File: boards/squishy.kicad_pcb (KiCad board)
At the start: 4 copper layers, 82 x 76.8 mm, 173 parts, among them J1 USB_B_Micro, J2 Conn_02x26_Top_Bottom, J3 Conn_02x05_Odd_Even, U1 128MiB, U10 THVD1451, U11 THVD1451, U12 THVD1451, U13 THVD1451, U14 THVD1451, U15 THVD1451, U16 THVD1451, U17 THVD1451, U18 THVD1451, U19 THVD1451, U2 ICE40HX8K-BG121, U20 THVD1451, U21 TXB0106, U22 TXB0106, U23 TXB0106, U24 TXB0106, U25 TXB0106, U26 TXB0106, U27 FT240XQ, U3 THVD1451, U4 THVD1451, U5 THVD1451, U6 THVD1451, U7 THVD1451, U8 THVD1451, U9 THVD1451, X1 ASEM-48MHz

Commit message: Routed the rest of the buses for the level shifters, added the bypass caps, and a whole bunch of other stuff
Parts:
- added C44: 0.1uF, Capacitor_SMD:C_0603_1608Metric, B.Cu at (156.3, 102.7)
- added C45: 0.1uF, Capacitor_SMD:C_0603_1608Metric, B.Cu at (146.8, 104.7)
- added C46: 0.1uF, Capacitor_SMD:C_0402_1005Metric, B.Cu at (147.8, 101.8)
- added C47: 0.1uF, Capacitor_SMD:C_0402_1005Metric, B.Cu at (150.9, 105.2)
- added C48: 0.1uF, Capacitor_SMD:C_0402_1005Metric, B.Cu at (148.0, 104.1)
- added C49: 0.1uF, Capacitor_SMD:C_0402_1005Metric, B.Cu at (149.7, 100.8)
- added C50: 0.1uF, Capacitor_SMD:C_0402_1005Metric, B.Cu at (150.8, 102.3)
- added C51: 0.1uF, Capacitor_SMD:C_0402_1005Metric, B.Cu at (153.2, 102.5)
- added C52: 0.1uF, Capacitor_SMD:C_0402_1005Metric, B.Cu at (151.4, 103.5)
- added C53: 0.1uF, Capacitor_SMD:C_0402_1005Metric, B.Cu at (148.7, 102.9)
- added D1: BLUE, LED_SMD:LED_0603_1608Metric_Pad1.05x0.95mm_HandSolder, F.Cu at (144.4, 117.8)
- added D10: BLUE, LED_SMD:LED_0603_1608Metric_Pad1.05x0.95mm_HandSolder, F.Cu at (154.9, 117.8)
- added D2: PINK, LED_SMD:LED_0603_1608Metric_Pad1.05x0.95mm_HandSolder, F.Cu at (146.2, 117.8)
- added D5: WHITE, LED_SMD:LED_0603_1608Metric_Pad1.05x0.95mm_HandSolder, F.Cu at (148.0, 117.8)
- added D6: PINK, LED_SMD:LED_0603_1608Metric_Pad1.05x0.95mm_HandSolder, F.Cu at (149.8, 117.8)
- added D9: BLUE, LED_SMD:LED_0603_1608Metric_Pad1.05x0.95mm_HandSolder, F.Cu at (151.6, 117.8)
- added R63: 4k7, Resistor_SMD:R_0603_1608Metric, F.Cu at (144.4, 114.5)
- added R64: 10k, Resistor_SMD:R_0603_1608Metric, F.Cu at (146.2, 114.5)
- added R65: 6k8, Resistor_SMD:R_0603_1608Metric, F.Cu at (148.0, 114.5)
- added R66: 10k, Resistor_SMD:R_0603_1608Metric, F.Cu at (149.8, 114.5)
- added R67: 4k7, Resistor_SMD:R_0603_1608Metric, F.Cu at (151.6, 114.5)
- added R68: 100k, Resistor_SMD:R_0603_1608Metric, B.Cu at (153.8, 107.2)
- added R69: 4k7, Resistor_SMD:R_0603_1608Metric, F.Cu at (154.9, 114.5)
- R11, R12, R14, R15, R17, R18, R20, R21, R23, R24, R26, R27, R29, R30, R32, R33, R35, R36, R38, R39, R41, R42, R44, R45, R47, R48, R50, R51, R53, R54, R56, R57, R59, R60, R62, R9: moved to B.Cu
- moved J3 50.2 mm to (176.5, 128.2)
- moved U1 25.4 mm to (161.1, 110.7), turned to 90 degrees
- moved C2 25.0 mm to (159.1, 107.1), turned to 90 degrees
- moved C25 3.40 mm to (126.7, 82.2)
- moved C27 3.40 mm to (147.4, 86.8)
- moved C28 3.40 mm to (157.8, 86.8)
- moved C29 3.40 mm to (147.4, 82.3)
- moved C30 3.40 mm to (157.8, 82.3)
- moved C31 3.40 mm to (168.2, 86.8)
- moved C32 3.40 mm to (178.7, 86.8)
- moved C33 3.40 mm to (168.2, 82.3)
- moved C34 3.40 mm to (178.7, 82.3)
- moved R10 3.40 mm to (127.8, 69.8)
- moved R13 3.40 mm to (124.3, 69.8)
- moved R16 3.40 mm to (120.9, 69.8)
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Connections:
- J3 pad 2: Net-(J3-Pad2) -> +3V3
- J3 pad 7: Net-(J3-Pad7) -> GND
- U1 pad 1: Net-(U1-Pad1) -> Net-(J3-Pad1)
- U1 pad 2: Net-(U1-Pad2) -> Net-(J3-Pad3)
- U1 pad 3: Net-(U1-Pad3) -> Net-(J3-Pad5)
- U1 pad 5: Net-(U1-Pad5) -> Net-(J3-Pad8)
- U1 pad 6: Net-(U1-Pad6) -> Net-(J3-Pad6)
- U1 pad 7: Net-(U1-Pad7) -> Net-(J3-Pad4)
- U2 pad A1: /DB1_TX -> /BNK0_OE
- U2 pad A10: /BSY_RX -> /MSG_RX
- U2 pad A11: /BNK1_OE -> /BNK3_OE
- U2 pad A2: /ATN_TX -> /DB0_TX
- U2 pad A4: /BNK0_OE -> /BNK1_OE
- U2 pad A5: /IO_RX -> /DB2_RX
- U2 pad A6: /DBP_TX -> /ACK_RX
- U2 pad A7: /REQ_RX -> /DB3_TX
- U2 pad A8: Net-(U2-PadA8) -> /DB4_RX
- U2 pad A9: /ACK_RX -> Net-(U2-PadA9)
- U2 pad B11: /BNK3_OE -> /MSG_TX
- U2 pad B3: /ATN_RX -> /ATN_TX
- U2 pad B4: /DB0_TX -> /DB1_TX
- U2 pad B5: /IO_TX -> /BSY_TX
- U2 pad B6: /DBP_RX -> /DB2_TX
- U2 pad B7: /REQ_TX -> /ACK_TX
- U2 pad B8: /DB2_TX -> /RST_TX
- U2 pad B9: /DB2_RX -> Net-(U2-PadB9)
- U2 pad C11: /MSG_RX -> /DB5_TX
- U2 pad C3: Net-(U2-PadC3) -> /DB0_RX
- U2 pad C4: Net-(U2-PadC4) -> /ATN_RX
- U2 pad C7: /BNK5_OE -> /DB3_RX
- U2 pad C8: /ACK_TX -> /RST_RX
- U2 pad C9: /BSY_TX -> /DB4_TX
- U2 pad D10: /MSG_TX -> /DB6_RX
- U2 pad D11: /DB5_RX -> /BNK4_OE
- U2 pad D5: /DB0_RX -> /BSY_RX
- U2 pad D7: Net-(U2-PadD7) -> /BNK2_OE
- U2 pad D9: /SEL_RX -> /DB5_RX
- U2 pad E10: /DB6_RX -> /CD_TX
- U2 pad E11: /DB5_TX -> /CD_RX
- U2 pad E8: /SEL_TX -> /SEL_RX
- U2 pad E9: /BNK4_OE -> /SEL_TX
- U2 pad F10: /CD_TX -> /DB7_TX
- U2 pad F11: /DB6_TX -> /DB7_RX
- U2 pad F9: /CD_RX -> /DB6_TX
- U2 pad G10: /BNK2_OE -> /REQ_TX
- U2 pad G11: /DB7_RX -> /REQ_RX
- U2 pad G8: /DB3_TX -> Net-(U2-PadG8)
- U2 pad G9: /DB7_TX -> /BNK5_OE
- U2 pad H1: Net-(U2-PadH1) -> /S1
- U2 pad H10: /RST_TX -> /DBP_TX
- U2 pad H11: /DB3_RX -> /DBP_RX
- U2 pad J1: Net-(U2-PadJ1) -> /S2
- U2 pad J10: /RST_RX -> /IO_TX
- U2 pad J11: /DB4_TX -> /IO_RX
- U2 pad J9: Net-(U1-Pad2) -> Net-(J3-Pad3)
- U2 pad K1: Net-(U2-PadK1) -> /S3
- U2 pad K10: Net-(U1-Pad1) -> Net-(J3-Pad1)
- U2 pad K11: /DB4_RX -> Net-(U2-PadK11)
- U2 pad K8: Net-(U2-PadK8) -> /FPGA_DONE
- U2 pad K9: Net-(U1-Pad5) -> Net-(J3-Pad8)
- U2 pad L1: Net-(U2-PadL1) -> /S4
- U2 pad L10: Net-(U1-Pad6) -> Net-(J3-Pad6)
- U2 pad L2: Net-(U2-PadL2) -> /S5
- U2 pad L9: Net-(U2-PadL9) -> /~FPGA_RESET
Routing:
- net /DB0_RX: track 4.61 -> 36.5 mm, vias 0 -> 2
- net /IO_TX: track 6.80 -> 38.4 mm
- net /ATN_RX: track 4.41 -> 35.9 mm, vias 0 -> 2
- net /DBP_TX: track 4.10 -> 34.3 mm
- net /ATN_TX: track 4.30 -> 34.4 mm
- net /BNK0_OE: track 7.68 -> 37.6 mm
- net /REQ_TX: track 4.10 -> 33.8 mm
- net /DB0_TX: track 4.51 -> 34.1 mm
- net /IO_RX: track 4.10 -> 33.6 mm
- net /DB1_TX: track 6.90 -> 36.1 mm
- net /DB1_RX: track 4.20 -> 33.2 mm
- net /DBP_RX: track 4.10 -> 33.1 mm
- net /BNK5_OE: track 8.38 -> 36.8 mm, vias 0 -> 2
- net /REQ_RX: track 4.10 -> 32.5 mm
- net /BNK1_OE: track 1.87 -> 27.9 mm
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- added copper zone on In2.Cu, net +1V2
- added copper zone on In1.Cu, net +3V3
- added copper zone on In2.Cu, net +3V3
- added copper zone on In1.Cu, net +5V
- added copper zone on In1.Cu, net GND
- added copper zone on In2.Cu, net GND

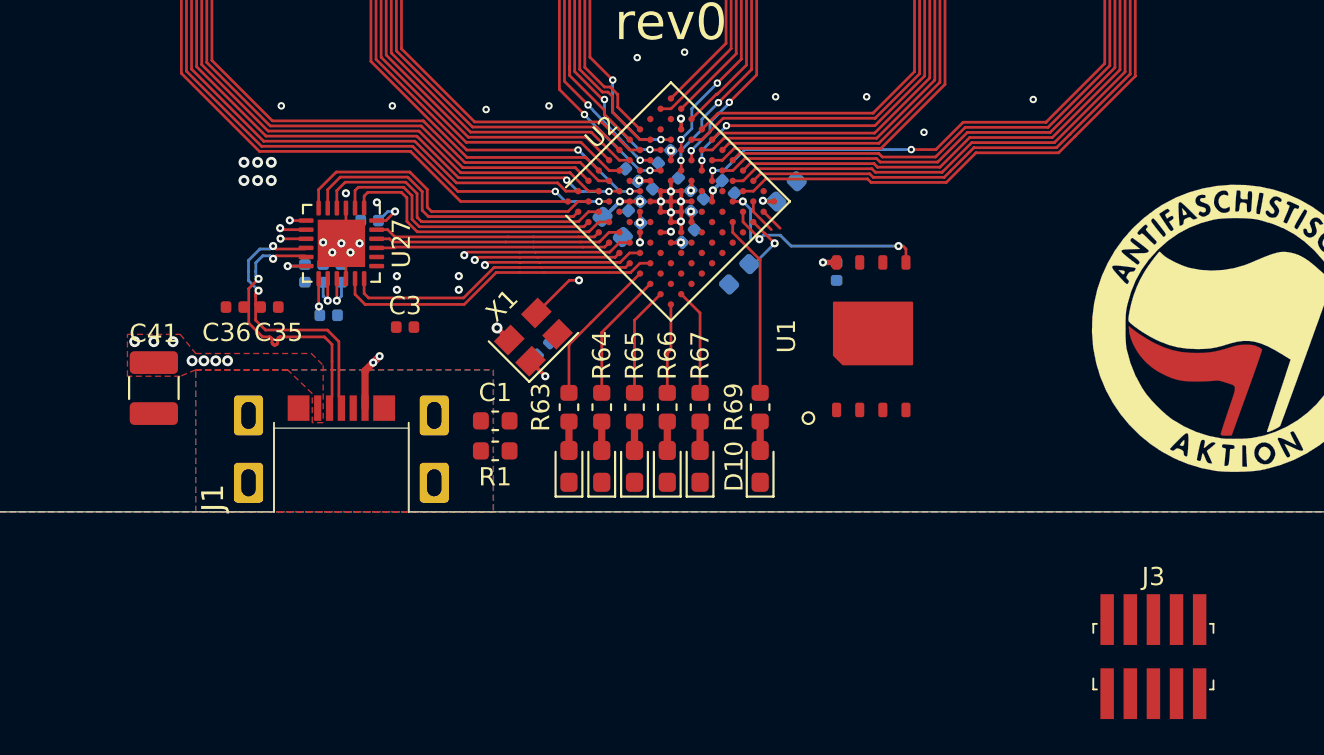
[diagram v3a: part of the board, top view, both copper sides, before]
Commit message: Completed the routing and power, the last two things to do are sort the SCSI TERMPOWER and DIFFSENSE, and then the FPGA reset.
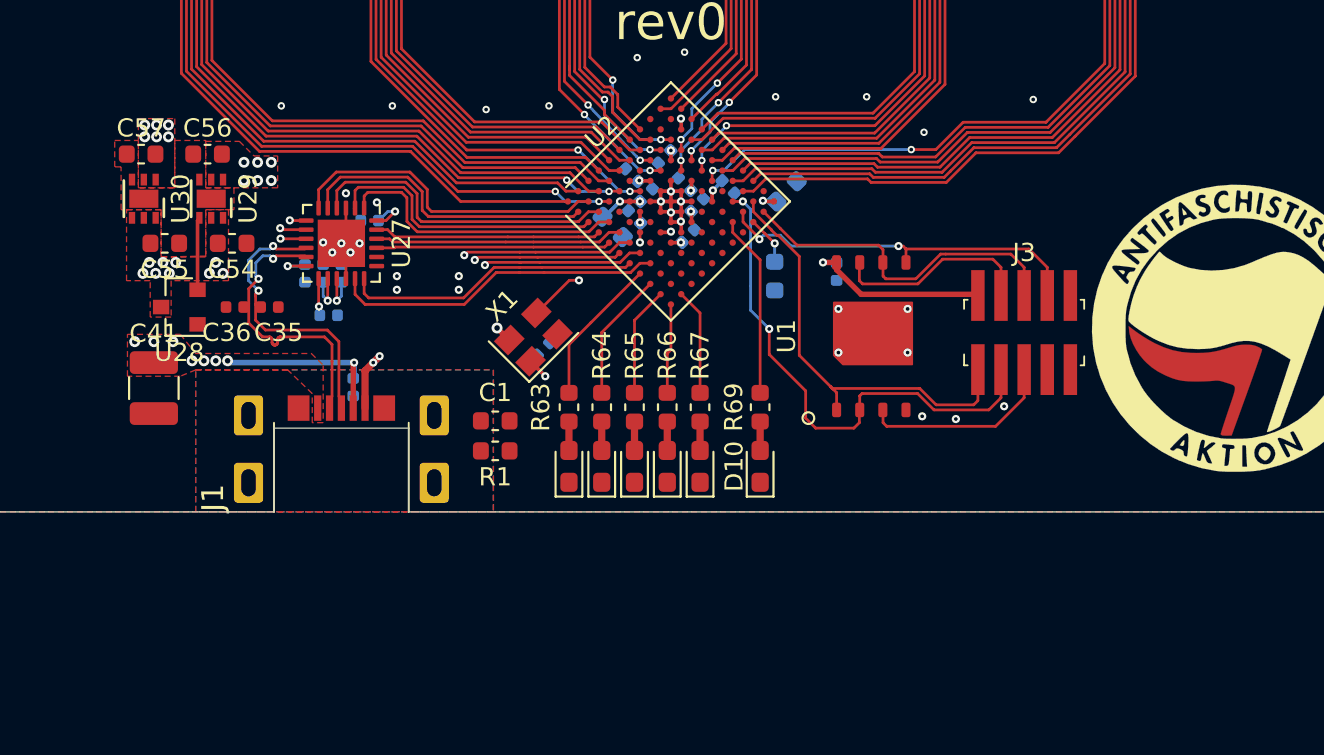
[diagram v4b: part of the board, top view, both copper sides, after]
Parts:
- added C54: 4.7uF, Capacitor_SMD:C_0603_1608Metric, F.Cu at (125.9, 105.5)
- added C55: 4.7uF, Capacitor_SMD:C_0603_1608Metric, F.Cu at (122.2, 105.5)
- added C56: 4.7uF, Capacitor_SMD:C_0603_1608Metric, F.Cu at (124.5, 100.7)
- added C57: 4.7uF, Capacitor_SMD:C_0603_1608Metric, F.Cu at (120.9, 100.7)
- added U28: MAX809JTRG, Package_TO_SOT_SMD:SOT-23, F.Cu at (123.0, 109.0)
- added U29: TLV755533PDRVR, Package_DFN_QFN:DFN-6-1EP_2x2mm_P0.65mm_EP1x1.6mm, F.Cu at (124.8, 103.1)
- added U30: TLV73312PQDRVRQ1, Package_DFN_QFN:DFN-6-1EP_2x2mm_P0.65mm_EP1x1.6mm, F.Cu at (121.0, 103.1)
- C3: moved to B.Cu
- C44, C45: value 0.1uF -> 4.7uF
- moved J3 19.2 mm to (169.4, 110.5)
- moved C3 4.36 mm to (132.6, 113.5), turned to 270 degrees
- moved R68 1.95 mm to (155.7, 107.3), turned to 90 degrees
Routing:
- net Net-(J3-Pad3): track 2.81 -> 28.6 mm, vias 1 -> 2
- net Net-(J3-Pad1): track 1.96 -> 23.7 mm
- net Net-(J3-Pad6): track 1.29 -> 19.0 mm
- net Net-(J3-Pad4): track 0.00 -> 11.1 mm
- net Net-(J3-Pad5): track 0.00 -> 10.7 mm
- net +5V: track 59.1 -> 69.4 mm, vias 49 -> 59
- net Net-(J3-Pad8): track 11.1 -> 20.8 mm
- net +3V3: track 30.1 -> 38.7 mm
- net Net-(U28-Pad2): track 0.00 -> 3.94 mm
- net /~FPGA_RESET: track 3.53 -> 2.78 mm
- net GND: vias 260 -> 267
- net +1V2: vias 5 -> 11
- added copper zone on F.Cu, net +1V2
- added copper zone on F.Cu, net +3V3
- removed copper zone on In2.Cu, net +3V3

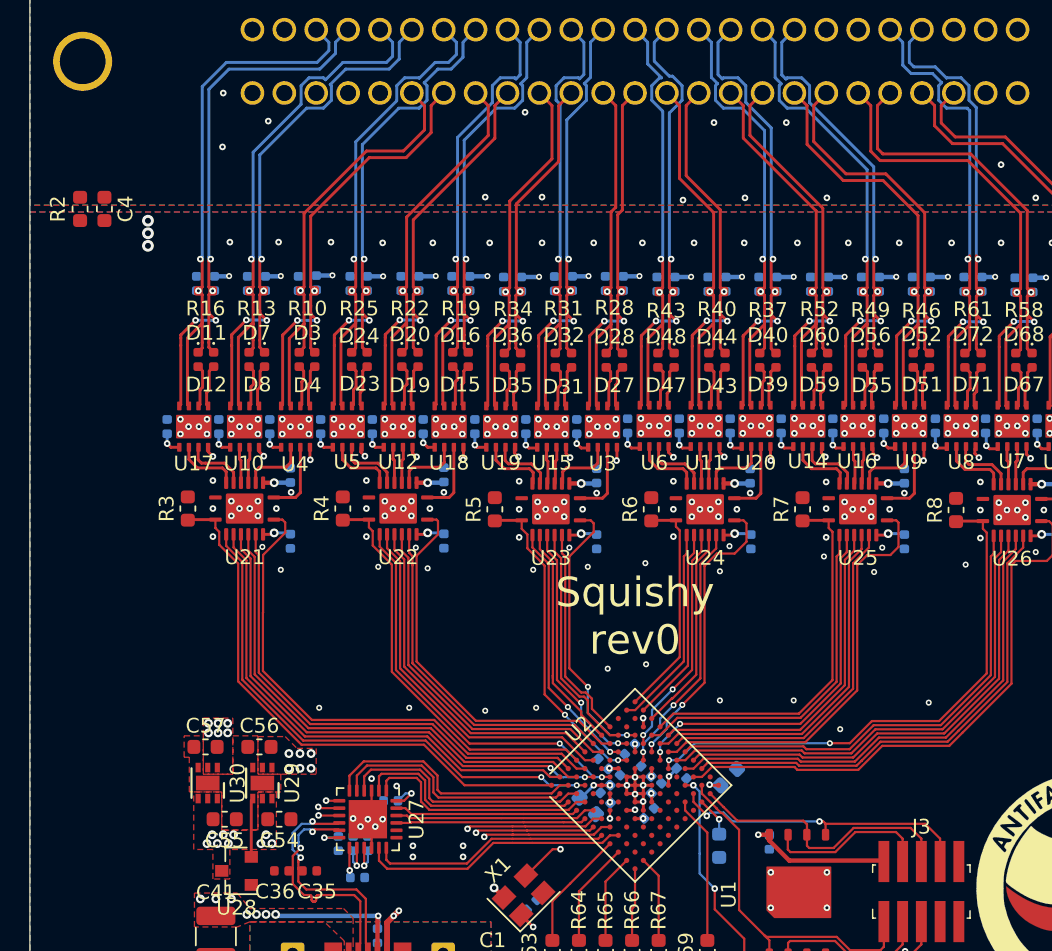
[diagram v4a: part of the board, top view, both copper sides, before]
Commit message: Added the needed bits for TERMPOWER and for the DIFFSENS line
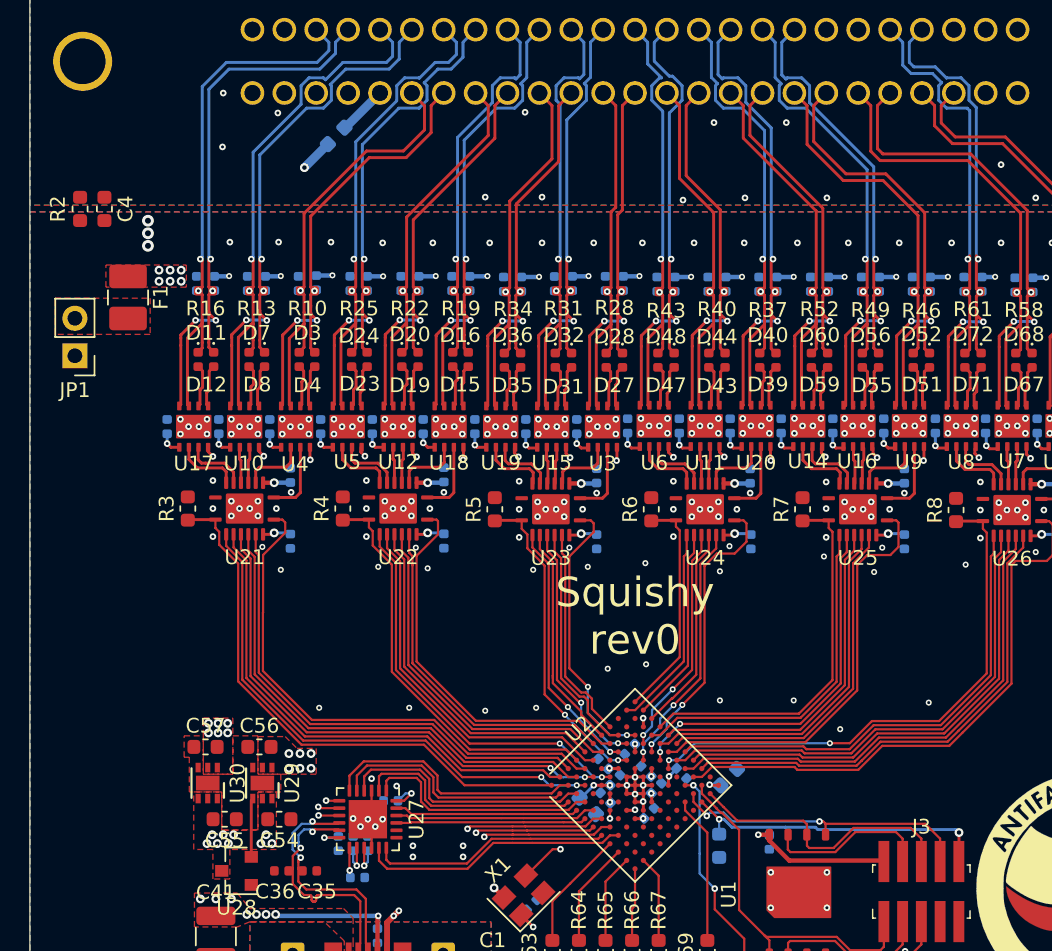
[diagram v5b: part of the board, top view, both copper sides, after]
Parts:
- added F1: Polyfuse_Small, Fuse:Fuse_1210_3225Metric_Castellated, F.Cu at (115.7, 70.2)
- added JP1: TERMPWR, Connector_PinHeader_2.54mm:PinHeader_1x02_P2.54mm_Vertical, F.Cu at (112.0, 74.2)
- added R70: 10k, Resistor_SMD:R_0603_1608Metric, B.Cu at (129.8, 59.2)
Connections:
- J3 pad 10: Net-(J3-Pad10) -> /~FPGA_RESET
- R12 pad 2: +5V -> /TERMPWR
- R15 pad 2: +5V -> /TERMPWR
- R18 pad 2: +5V -> /TERMPWR
- R21 pad 2: +5V -> /TERMPWR
- R24 pad 2: +5V -> /TERMPWR
- R27 pad 2: +5V -> /TERMPWR
- R30 pad 2: +5V -> /TERMPWR
- R33 pad 2: +5V -> /TERMPWR
- R36 pad 2: +5V -> /TERMPWR
- R39 pad 2: +5V -> /TERMPWR
- R42 pad 2: +5V -> /TERMPWR
- R45 pad 2: +5V -> /TERMPWR
- R48 pad 2: +5V -> /TERMPWR
- R51 pad 2: +5V -> /TERMPWR
- R54 pad 2: +5V -> /TERMPWR
- R57 pad 2: +5V -> /TERMPWR
- R60 pad 2: +5V -> /TERMPWR
- R9 pad 2: +5V -> /TERMPWR
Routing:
- net /TERMPWR: track 0.00 -> 21.9 mm, vias 0 -> 25
- net +5V: track 69.4 -> 49.8 mm, vias 59 -> 41
- net /~FPGA_RESET: track 2.78 -> 21.3 mm, vias 1 -> 2
- net /DIFF_SENSE: track 0.00 -> 3.40 mm
- added copper zone on F.Cu, net /TERMPWR
- added copper zone on In2.Cu, net /TERMPWR
- added copper zone on F.Cu, net Net-(F1-Pad2)

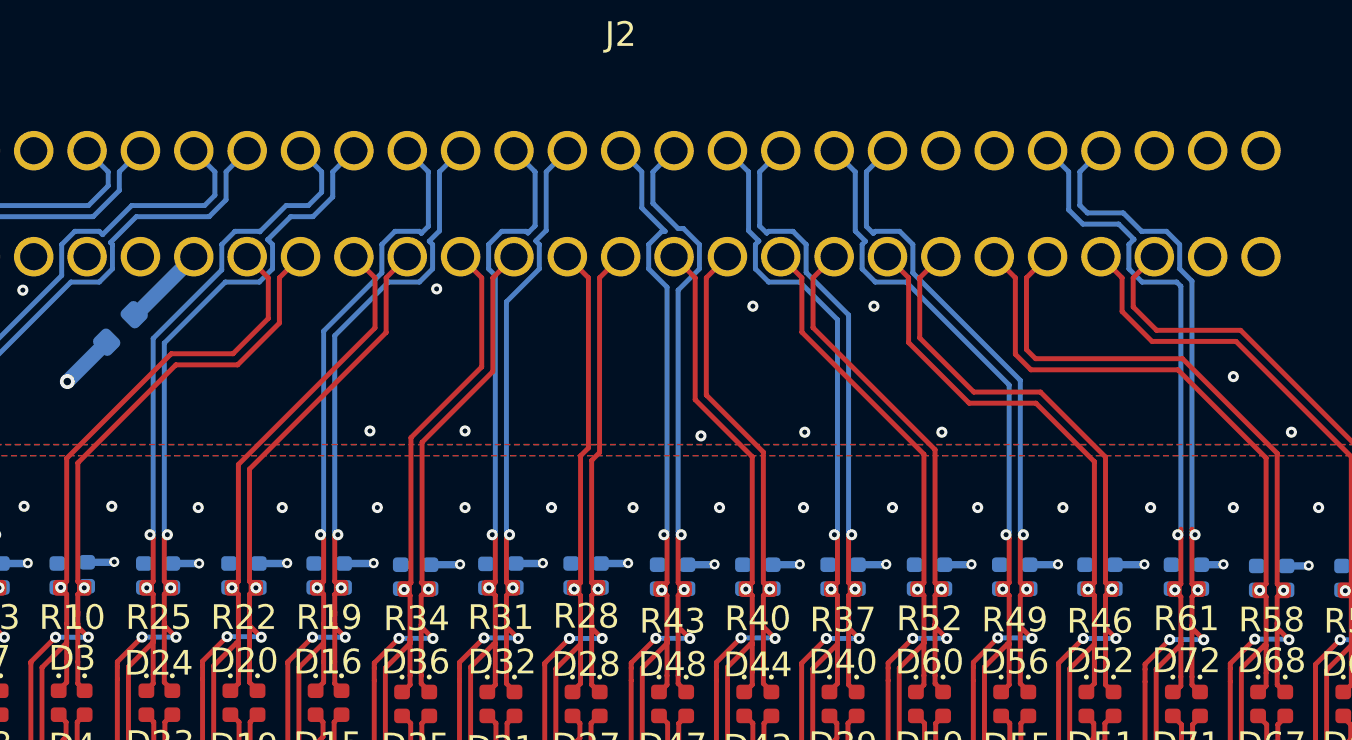
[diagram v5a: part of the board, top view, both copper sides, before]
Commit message: Skew-matched most of the diff-pairs
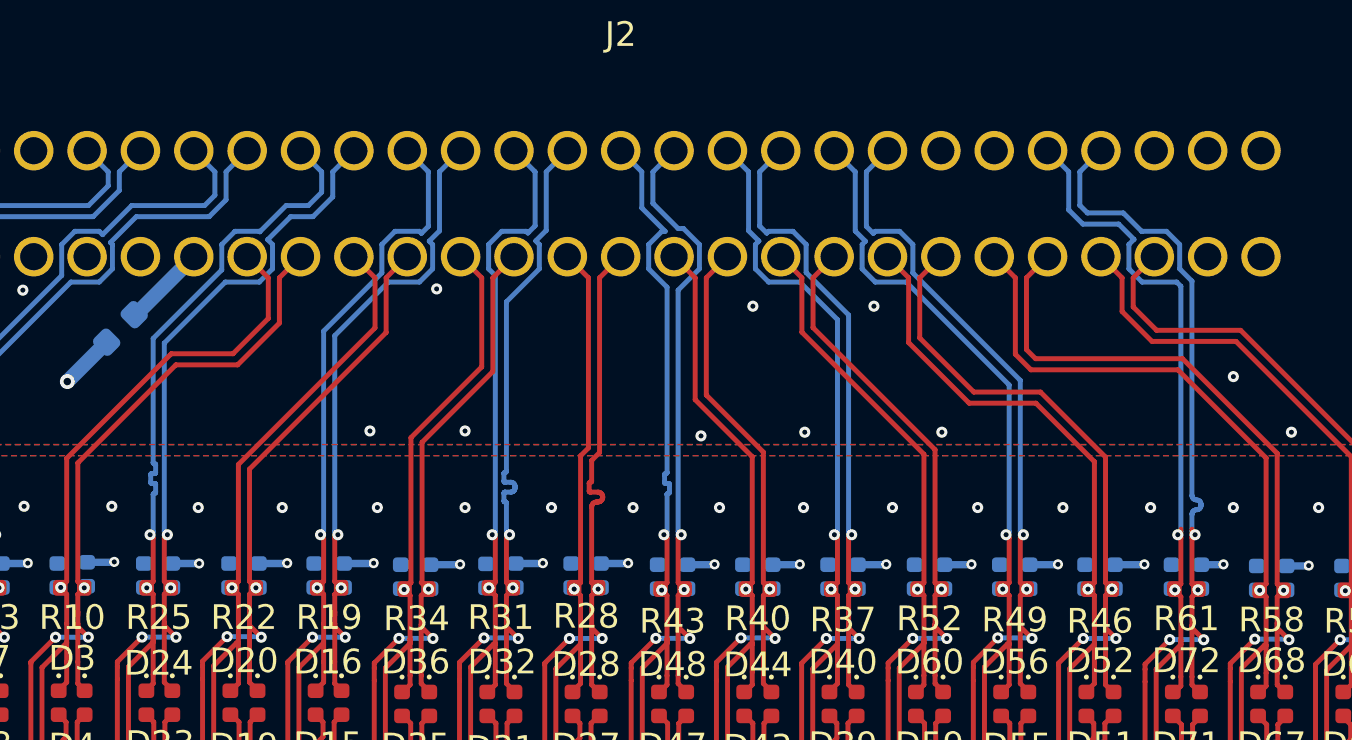
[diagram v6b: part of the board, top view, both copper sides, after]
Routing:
- net /MSG+: track 32.4 -> 33.2 mm
- net /DB5+: track 26.7 -> 27.5 mm

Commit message: Updates to the schematic, REV0 is "done"
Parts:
- added FID1: Fiducial, Fiducial:Fiducial_0.75mm_Mask1.5mm, F.Cu at (113.0, 47.5)
- added FID2: Fiducial, Fiducial:Fiducial_0.75mm_Mask1.5mm, F.Cu at (187.0, 47.5)
- added FID3: Fiducial, Fiducial:Fiducial_0.75mm_Mask1.5mm, F.Cu at (113.0, 116.3)
- added FID4: Fiducial, Fiducial:Fiducial_0.75mm_Mask1.5mm, B.Cu at (113.0, 116.3)
- added FID5: Fiducial, Fiducial:Fiducial_0.75mm_Mask1.5mm, B.Cu at (187.0, 47.5)
- added FID6: Fiducial, Fiducial:Fiducial_0.75mm_Mask1.5mm, B.Cu at (113.0, 47.5)
- added R71: 10k, Resistor_SMD:R_0603_1608Metric, B.Cu at (157.1, 108.2)
- added TP1: 1v2, TestPoint:TestPoint_Pad_D1.0mm, F.Cu at (119.7, 98.9)
- added TP2: 5v0, TestPoint:TestPoint_Pad_D1.0mm, F.Cu at (119.0, 105.5)
- added TP3: 3v3, TestPoint:TestPoint_Pad_D1.0mm, F.Cu at (123.8, 98.9)
- added TP4: GND, TestPoint:TestPoint_Pad_D1.0mm, F.Cu at (117.0, 114.9)
- R68: value 100k -> 10k; moved to F.Cu
- moved R68 0.05 mm to (155.7, 107.4), turned to 270 degrees
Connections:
- R68 pad 1: GND -> /~FPGA_RESET
- R68 pad 2: /~FPGA_RESET -> +3V3
- U2 pad A9: Net-(U2-PadA9) -> /DIFF_SENSE
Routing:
- net /DIFF_SENSE: track 3.40 -> 60.1 mm, vias 0 -> 1
- net +3V3: track 38.7 -> 44.8 mm, vias 26 -> 27
- net +5V: track 49.8 -> 51.1 mm
- net +1V2: track 4.92 -> 6.17 mm
- net Net-(J3-Pad1): vias 0 -> 1
- net GND: vias 267 -> 269
- net /SHIELD: vias 13 -> 16
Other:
- board text added: "FAUX-SCSI TRANSCEIVER"
- board text added: "JLCJLCJLCJLCJLC"
- board text added: "SCSI-1 HVD ONLY"
- board text added: "TERMPWR"
